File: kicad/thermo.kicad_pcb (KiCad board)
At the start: 2 copper layers, 70 x 50 mm, 59 parts, among them P1 CONN_VREF, P10 CONN_STM32F030_11_20, P11 CONN_HD44780, P12 CONN_BAT, P13 TP_GND, P14 TP_5V, P15 TP_3V, P16 TP_THERM_OUT, P17 TP_MULT_OUT, P18 TP_VREF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

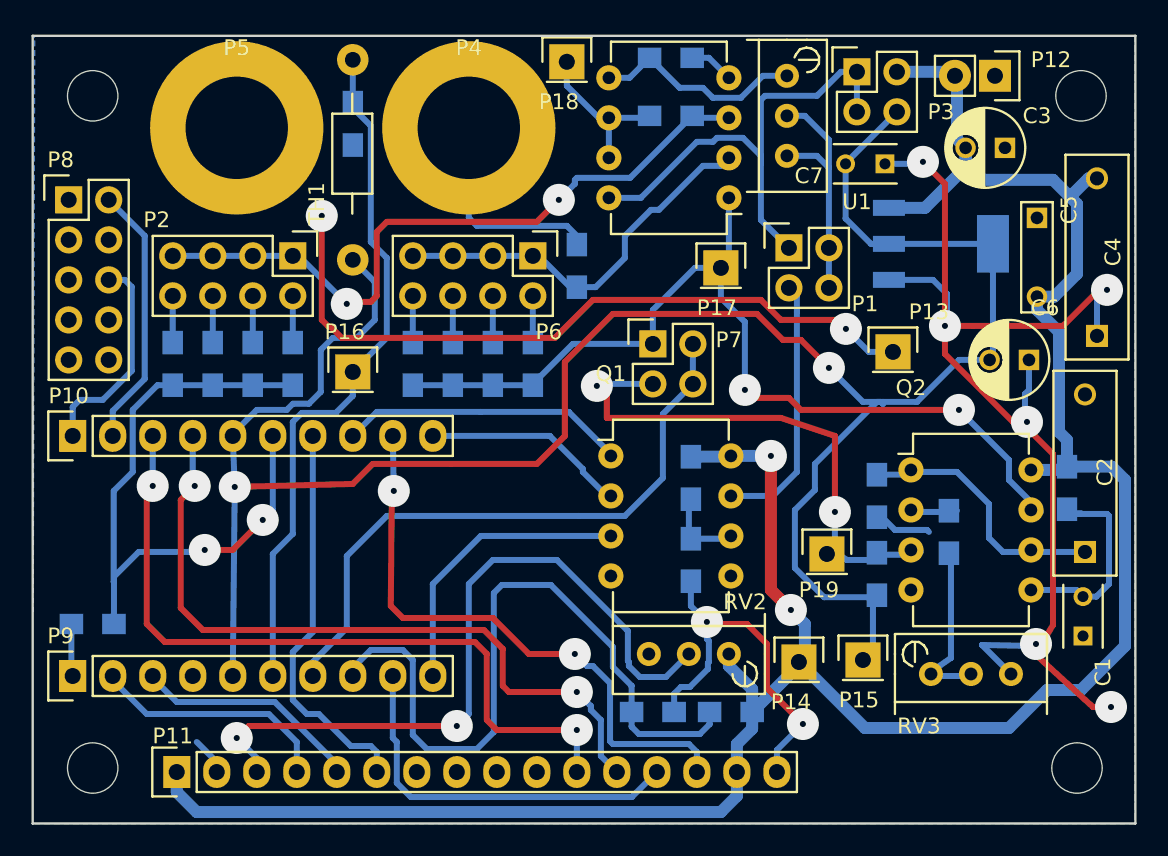
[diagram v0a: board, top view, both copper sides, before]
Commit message: Fix Vss and Vdd swapped on display connector
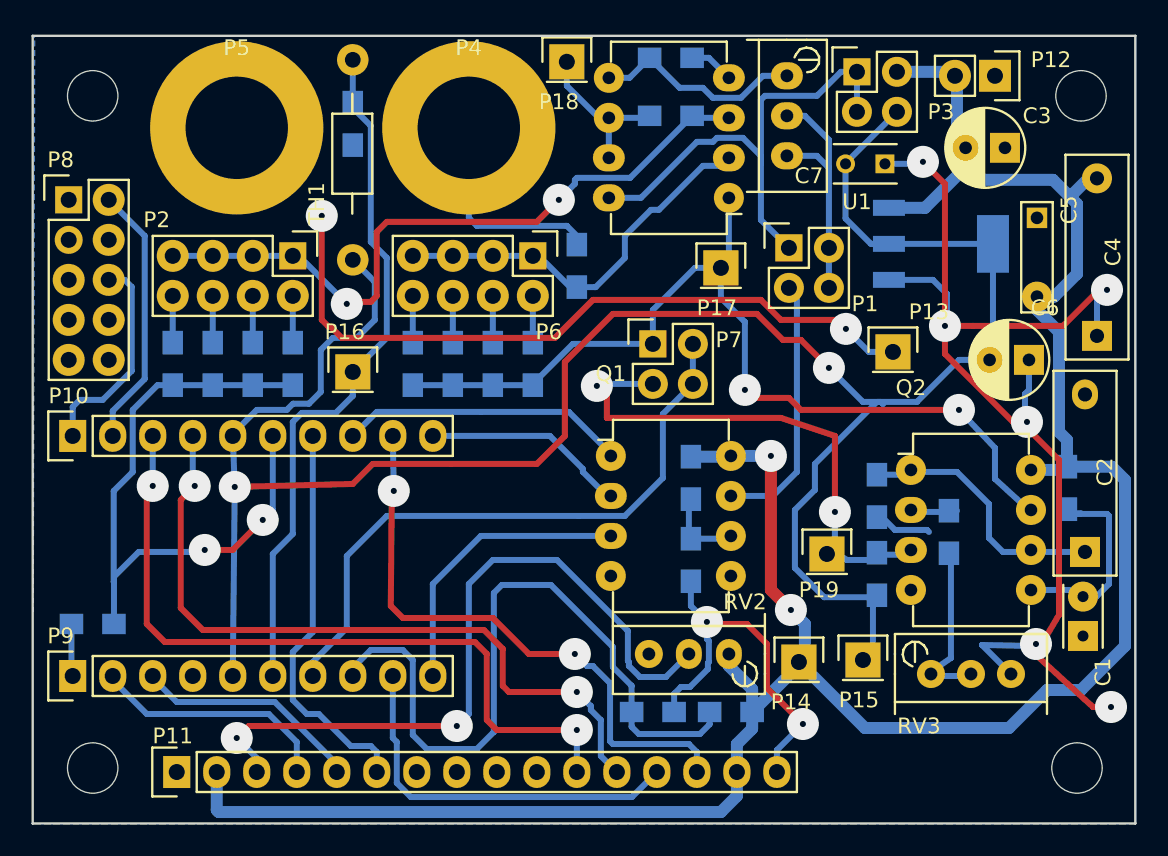
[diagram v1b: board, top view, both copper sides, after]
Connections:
- P11 pad 1: +5V -> GND
- P11 pad 2: GND -> +5V
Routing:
- net GND: track 196.3 -> 194.2 mm
- net +5V: track 160.1 -> 158.8 mm
